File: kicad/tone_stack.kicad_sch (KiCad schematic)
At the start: 4 parts

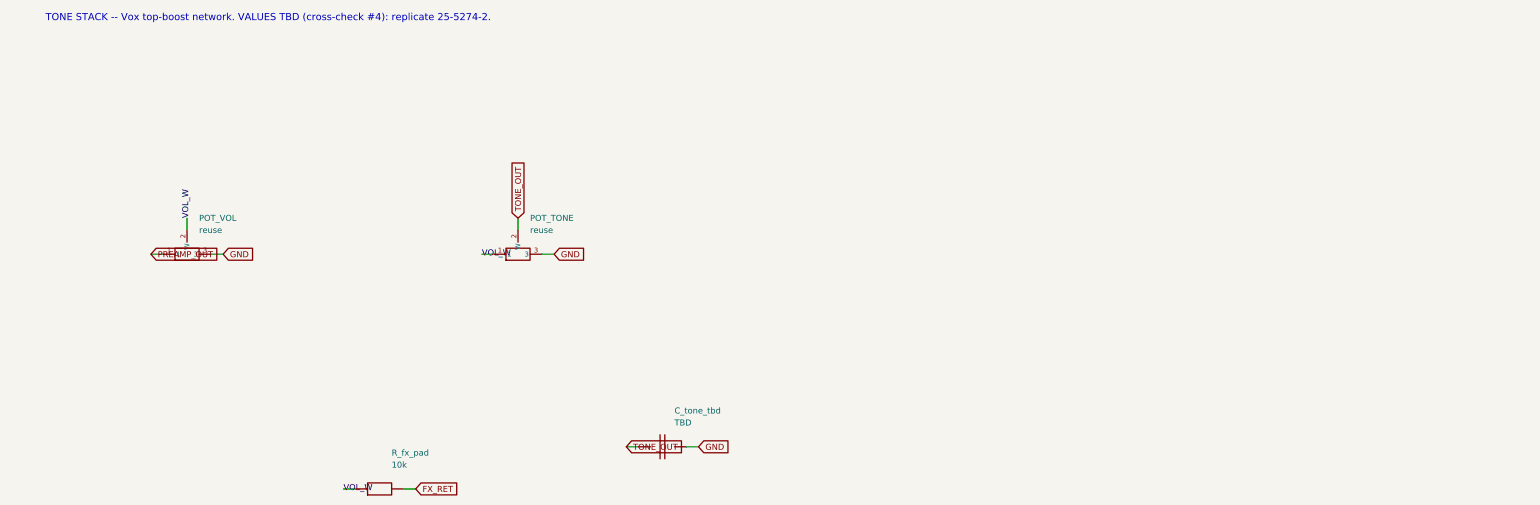
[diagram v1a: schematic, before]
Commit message: Design + verify the tone stack (Vox treble-cut substitute)
The tone sheet was a TBD placeholder (original 25-5274-2 values never recovered).
Replaced with a working passive Vox-style control: Volume pot + a treble "cut"
(C_cut 10nF + POT_TONE 100k to ground). Verified in spice/ac_tonestack.cir:
flat at bright (-1.6 dB, just insertion loss), musical treble cut at the dark end
(-9 dB @ 5 kHz, -14 dB @ 10 kHz). Clearly flagged as a designed substitute (the
original panel may have had separate Treble/Bass) in the sheet note, cross-check
#4, and spice/README.

All 7 ngspice blocks now pass (added ac_tonestack.cir). ERC 0, demo DRC 0, BOM
regenerated from the schematic (no TBD rows left).

https://claude.ai/code/session_01PkrfUi9tvZfLvudJ7h23qD
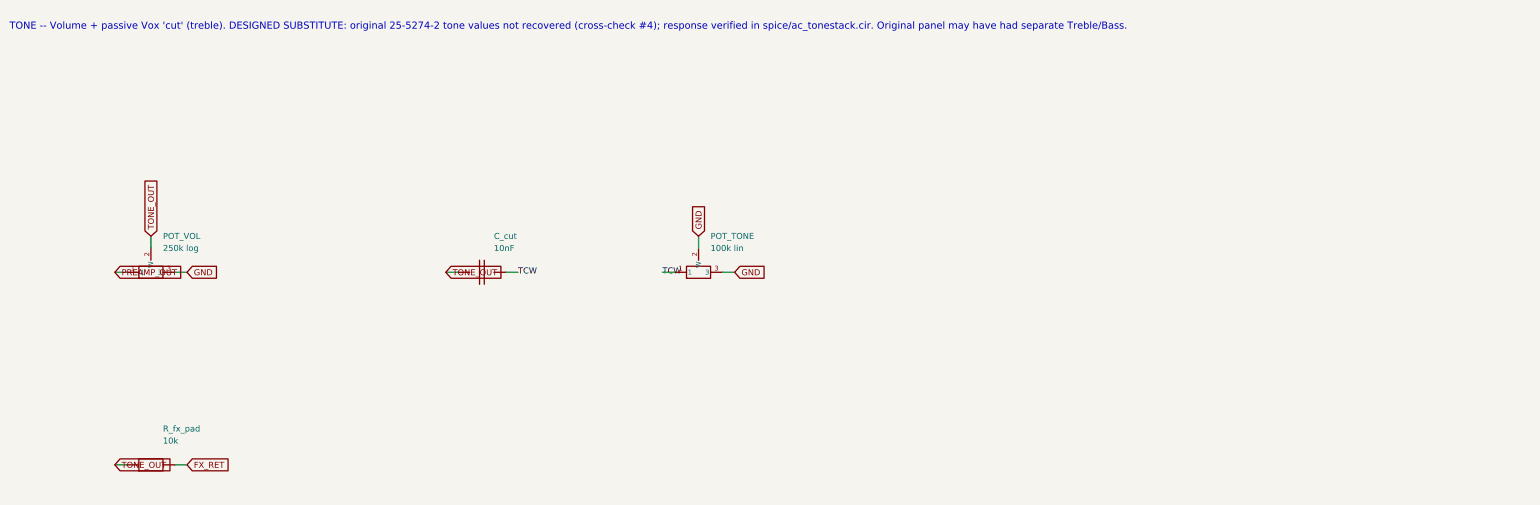
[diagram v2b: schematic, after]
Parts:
- removed C_tone_tbd: TBD, Capacitor_THT:C_Disc_D7.5mm_W2.5mm_P5.00mm, symbol cr_primitives:C
- added C_cut: 10nF, Capacitor_THT:C_Disc_D7.5mm_W2.5mm_P5.00mm, symbol cr_primitives:C
- POT_TONE: value reuse -> 100k lin
- POT_VOL: value reuse -> 250k log
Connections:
- net GND: now also POT_TONE.2 (W)
- net TONE_OUT: now also POT_VOL.2 (W), R_fx_pad.1, C_cut.1; no longer POT_TONE.2 (W)
- removed net VOL_W: POT_TONE.1, POT_VOL.2 (W), R_fx_pad.1
- new net TCW: C_cut.2, POT_TONE.1
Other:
- note added: "TONE -- Volume + passive Vox 'cut' (treble). DESIGNED SUBSTITUTE: original 25-5274-2 tone values not recovered (cross-check #4); response verified in spice/ac_tonestack.cir. Original panel may have had separate Treble/Bass."
- note removed: "TONE STACK -- Vox top-boost network. VALUES TBD (cross-check #4): replicate 25-5274-2."
